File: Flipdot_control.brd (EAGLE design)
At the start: 160 x 100 mm, 24 parts, among them IC1 ULN2003, IC10 ULN2003, IC11 M74HC238, IC12 M74HC238, IC13 M74HC238, IC14 TD62783_AFWG, IC15 ULN2003, IC16 TD62783_AFWG, IC17 ULN2003, IC18 M74HC238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

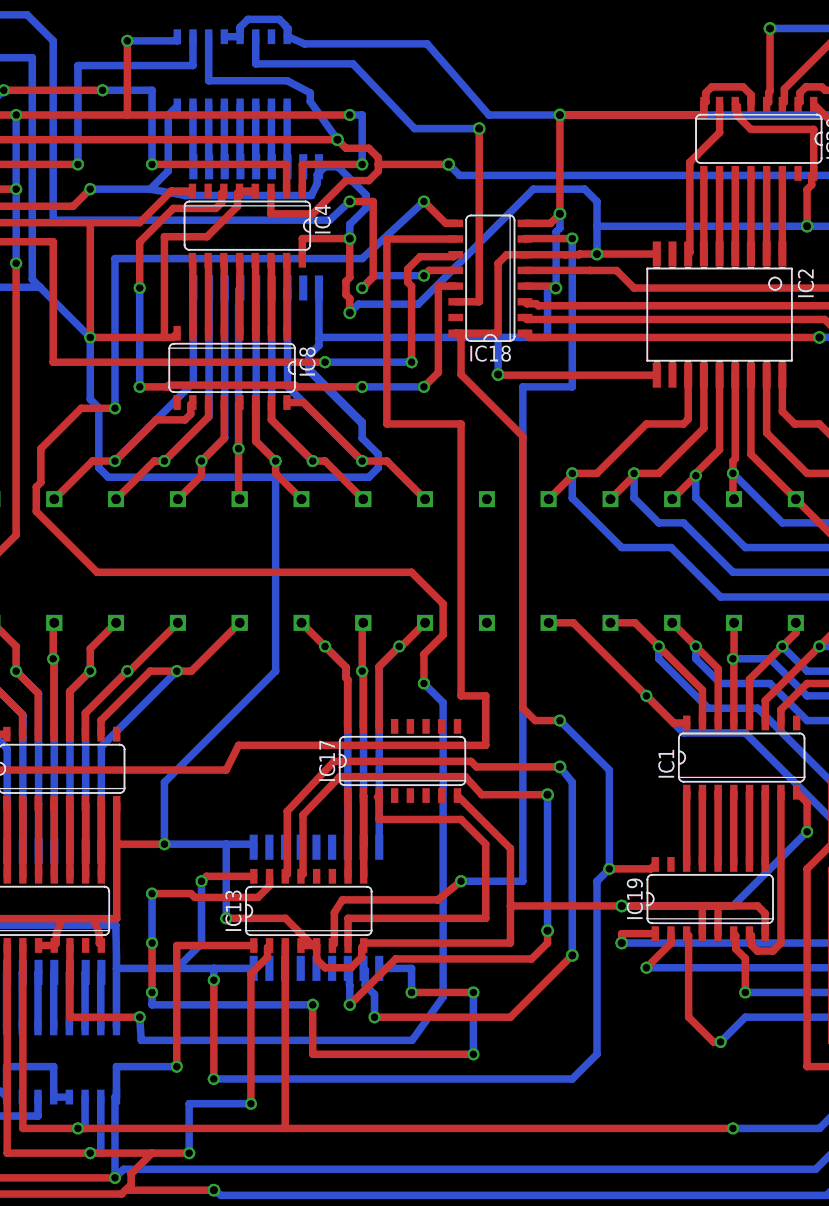
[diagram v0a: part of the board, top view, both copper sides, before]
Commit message: Fixed airwires
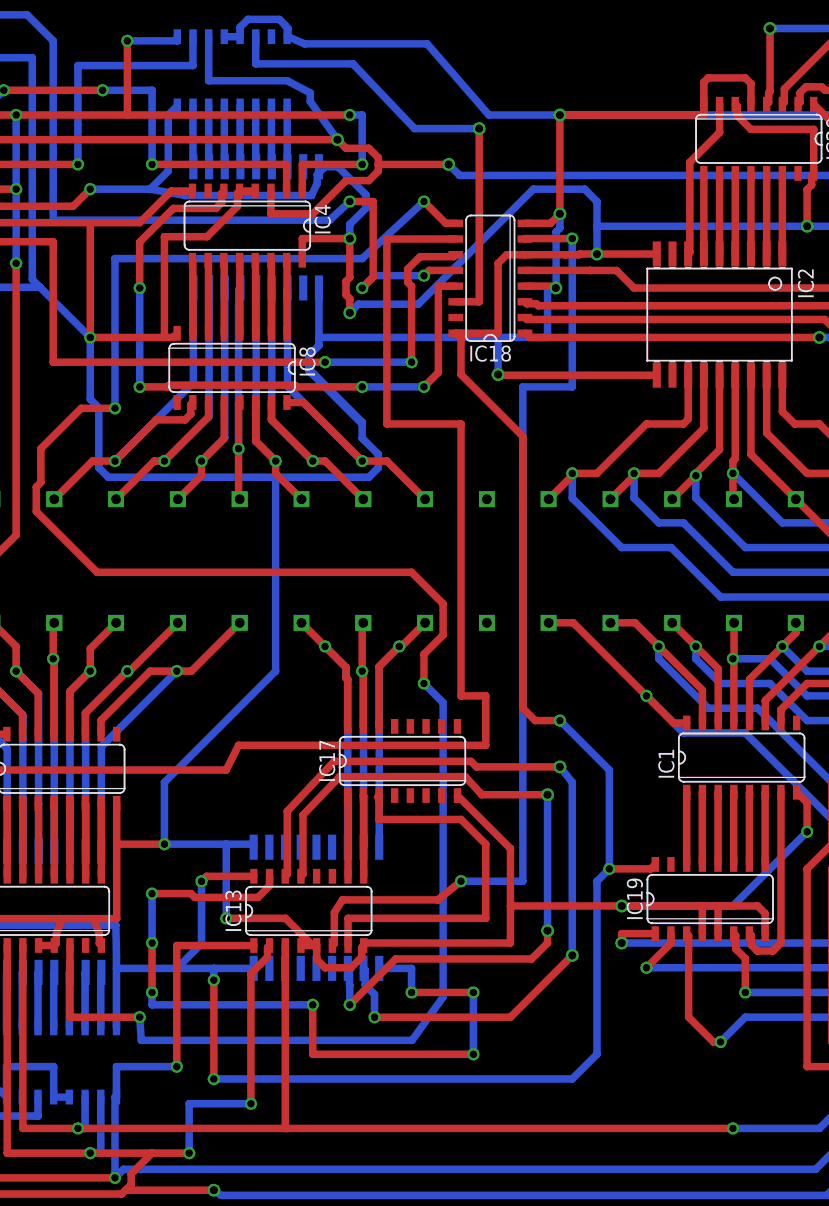
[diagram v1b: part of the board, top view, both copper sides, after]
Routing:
- net GND: track 642.8 -> 644.6 mm
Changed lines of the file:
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@@
 <contactref element="IC20" pad="8"/>
 <contactref element="IC20" pad="5"/>
-<wire x1="87.649" y1="90" x2="87.649" y2="90.873" width="0.6096" layer="1"/>
-<wire x1="87.8142" y1="91.80635625" x2="88.28564375" y2="92.2778" width="0.6096" layer="1"/>
-<wire x1="87.649" y1="90.873" x2="87.8142" y2="91.0382" width="0.6096" layer="1"/>
-<wire x1="87.8142" y1="91.0382" x2="87.8142" y2="91.80635625" width="0.6096" layer="1"/>
-<wire x1="88.28564375" y1="92.2778" x2="90.82235625" y2="92.2778" width="0.6096" layer="1"/>
-<wire x1="90.82235625" y1="92.2778" x2="91.4638" y2="91.63635625" width="0.6096" layer="1"/>
-<wire x1="91.4638" y1="91.63635625" x2="91.4638" y2="90.873" width="0.6096" layer="1"/>
+<wire x1="87.649" y1="90.873" x2="87.649" y2="90" width="0.6096" layer="1"/>
 <wire x1="31.23" y1="13" x2="31.23" y2="10.535" width="0.6096" layer="16"/>
 <wire x1="35.04" y1="10.535" x2="35.04" y2="13" width="0.6096" layer="16"/>
@@
 <wire x1="153" y1="83" x2="136" y2="83" width="0.6096" layer="16"/>
 <wire x1="136" y1="83" x2="136" y2="78.04" width="0.6096" layer="16"/>
-<wire x1="91.4638" y1="90.873" x2="91.459" y2="90.873" width="0" layer="19" extent="1-1"/>
+<wire x1="91.459" y1="90.873" x2="91.459" y2="92.541" width="0.6096" layer="1"/>
+<wire x1="91.459" y1="92.541" x2="91" y2="93" width="0.6096" layer="1"/>
+<wire x1="91" y1="93" x2="88" y2="93" width="0.6096" layer="1"/>
+<wire x1="88" y1="93" x2="87.649" y2="92.649" width="0.6096" layer="1"/>
+<wire x1="87.649" y1="92.649" x2="87.649" y2="90.873" width="0.6096" layer="1"/>
 </signal>
 <signal name="R7H">
@@
 <contactref element="IC2" pad="7"/>
 <wire x1="86.379" y1="78.7512" x2="86.514" y2="78.8862" width="0.6096" layer="1"/>
-<wire x1="88.9238" y1="88.58595625" x2="88.9238" y2="90.873" width="0.6096" layer="1"/>
 <wire x1="86.514" y1="78.8862" x2="86.514" y2="86.17615625" width="0.6096" layer="1"/>
-<wire x1="86.514" y1="86.17615625" x2="88.9238" y2="88.58595625" width="0.6096" layer="1"/>
-<wire x1="88.9238" y1="90.873" x2="88.919" y2="90.873" width="0" layer="19" extent="1-1"/>
+<wire x1="88.9238" y1="88.58595625" x2="86.514" y2="86.17615625" width="0.6096" layer="1"/>
+<wire x1="88.919" y1="90.873" x2="88.9238" y2="90.8682" width="0.6096" layer="1"/>
+<wire x1="88.9238" y1="90.8682" x2="88.9238" y2="88.58595625" width="0.6096" layer="1"/>
 </signal>
 <signal name="RE">
@@
 <wire x1="37" y1="8" x2="37.58" y2="8" width="0.6096" layer="16"/>
 <wire x1="37.58" y1="8" x2="37.58" y2="10.535" width="0.6096" layer="16"/>
-<wire x1="37" y1="8" x2="53.7732" y2="8" width="0.6096" layer="1"/>
-<wire x1="53.7732" y1="8" x2="53.7732" y2="22.799" width="0.6096" layer="1"/>
-<wire x1="53.7732" y1="8" x2="90" y2="8" width="0.6096" layer="1"/>
+<wire x1="54" y1="8" x2="37" y2="8" width="0.6096" layer="1"/>
+<wire x1="54" y1="8" x2="90" y2="8" width="0.6096" layer="1"/>
 <wire x1="121" y1="50" x2="121" y2="51.8727625" width="0.6096" layer="1"/>
 <wire x1="121" y1="51.8727625" x2="120.9554" y2="51.9173625" width="0.6096" layer="1"/>
@@
 <wire x1="152" y1="47" x2="154" y2="49" width="0.6096" layer="16"/>
 <wire x1="154" y1="49" x2="154" y2="49.78" width="0.6096" layer="16"/>
-<wire x1="53.7732" y1="22.799" x2="53.778" y2="22.799" width="0" layer="19" extent="1-1"/>
+<wire x1="53.778" y1="22.799" x2="53.778" y2="8" width="0.6096" layer="1"/>
+<wire x1="53.778" y1="8" x2="54" y2="8" width="0.6096" layer="1"/>
 </signal>
 <signal name="E1">

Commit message: Fucked up, fixed
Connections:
- net 12V: now also IC14.9, IC16.9, IC2.9, IC7.9, IC9.9
- net 5V: no longer IC14.9, IC16.9, IC2.9, IC7.9, IC9.9
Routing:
- net 12V: track 42.9 -> 377.1 mm, vias 2 -> 11
- net B: track 477.0 -> 449.4 mm, vias 14 -> 13
- net 5V: track 441.8 -> 458.9 mm, vias 21 -> 22
- net RE: track 148.8 -> 154.1 mm
- net C: track 396.7 -> 399.4 mm
- net A: track 430.0 -> 430.8 mm

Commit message: Finished segment schematic, fixed some errors
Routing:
- net 5V: track 458.9 -> 446.8 mm, vias 22 -> 21
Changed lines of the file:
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@@
 <layer number="19" name="Unrouted" color="6" fill="1" visible="yes" active="yes"/>
 <layer number="20" name="Dimension" color="15" fill="1" visible="yes" active="yes"/>
-<layer number="21" name="tPlace" color="7" fill="1" visible="no" active="yes"/>
+<layer number="21" name="tPlace" color="7" fill="1" visible="yes" active="yes"/>
 <layer number="22" name="bPlace" color="7" fill="1" visible="yes" active="yes"/>
-<layer number="23" name="tOrigins" color="15" fill="1" visible="no" active="yes"/>
+<layer number="23" name="tOrigins" color="15" fill="1" visible="yes" active="yes"/>
 <layer number="24" name="bOrigins" color="15" fill="1" visible="yes" active="yes"/>
-<layer number="25" name="tNames" color="7" fill="1" visible="no" active="yes"/>
+<layer number="25" name="tNames" color="7" fill="1" visible="yes" active="yes"/>
 <layer number="26" name="bNames" color="7" fill="1" visible="yes" active="yes"/>
-<layer number="27" name="tValues" color="7" fill="1" visible="no" active="yes"/>
+<layer number="27" name="tValues" color="7" fill="1" visible="yes" active="yes"/>
 <layer number="28" name="bValues" color="7" fill="1" visible="yes" active="yes"/>
 <layer number="29" name="tStop" color="7" fill="3" visible="no" active="yes"/>
@@
 <layer number="38" name="bTest" color="7" fill="1" visible="no" active="yes"/>
 <layer number="39" name="tKeepout" color="4" fill="11" visible="no" active="yes"/>
-<layer number="40" name="bKeepout" color="1" fill="11" visible="yes" active="yes"/>
+<layer number="40" name="bKeepout" color="1" fill="11" visible="no" active="yes"/>
 <layer number="41" name="tRestrict" color="4" fill="10" visible="no" active="yes"/>
-<layer number="42" name="bRestrict" color="1" fill="10" visible="yes" active="yes"/>
+<layer number="42" name="bRestrict" color="1" fill="10" visible="no" active="yes"/>
 <layer number="43" name="vRestrict" color="2" fill="10" visible="no" active="yes"/>
-<layer number="44" name="Drills" color="7" fill="1" visible="yes" active="yes"/>
-<layer number="45" name="Holes" color="7" fill="1" visible="yes" active="yes"/>
+<layer number="44" name="Drills" color="7" fill="1" visible="no" active="yes"/>
+<layer number="45" name="Holes" color="7" fill="1" visible="no" active="yes"/>
 <layer number="46" name="Milling" color="3" fill="1" visible="no" active="yes"/>
 <layer number="47" name="Measures" color="7" fill="1" visible="no" active="yes"/>
@@
 <layer number="49" name="Reference" color="7" fill="1" visible="no" active="yes"/>
 <layer number="50" name="dxf" color="7" fill="1" visible="no" active="no"/>
-<layer number="51" name="tDocu" color="7" fill="1" visible="no" active="yes"/>
+<layer number="51" name="tDocu" color="7" fill="1" visible="yes" active="yes"/>
 <layer number="52" name="bDocu" color="7" fill="1" visible="yes" active="yes"/>
 <layer number="53" name="tGND_GNDA" color="7" fill="9" visible="no" active="no"/>
@@
 <wire x1="30" y1="78" x2="30" y2="80.9682" width="0.6096" layer="16"/>
 <wire x1="30" y1="80.9682" x2="28.352203125" y2="82.615996875" width="0.6096" layer="16"/>
-<via x="25.127" y="89.508" extent="1-16" drill="0.6"/>
-<wire x1="13" y1="89.508" x2="25.127" y2="89.508" width="0.6096" layer="1"/>
 <via x="13" y="89.508" extent="1-16" drill="0.6"/>
 <wire x1="13" y1="89.508" x2="13" y2="90.379" width="0.6096" layer="16"/>

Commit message: Starting again [backup]
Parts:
- added U$1: PS, Flipdot:PS
- moved J1 14.0 mm to (46.1, 52.9)
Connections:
- net 12V: now also U$1.P$1, U$1.P$2
- net GND: now also U$1.P$3
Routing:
- net E6: track 163.6 -> 110.6 mm, vias 4 -> 3
- net A: track 430.8 -> 381.9 mm
- net E7: track 78.9 -> 38.9 mm
- net R5L: track 82.5 -> 119.8 mm
- net R4L: track 78.5 -> 115.2 mm
- net R6L: track 87.9 -> 124.3 mm
- net R3L: track 76.4 -> 112.3 mm
- net R7L: track 92.6 -> 126.9 mm
- net E5: track 147.1 -> 113.1 mm
- net R4H: track 111.1 -> 143.1 mm
- net 5V: track 446.8 -> 416.3 mm
- net R3H: track 116.0 -> 145.7 mm
- net R2L: track 88.3 -> 115.5 mm, vias 3 -> 4
- net R2H: track 119.3 -> 146.3 mm
- net R1L: track 101.3 -> 126.9 mm, vias 5 -> 6
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
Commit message: Finished new design
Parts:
- moved U$1 91.7 mm to (101.6, 9.63), turned to 90 degrees
- moved J2 67.3 mm to (84.4, 50.8), flipped to the bottom, turned to 180 degrees
- moved IC21 52.8 mm to (98.1, 62.0), turned to 0 degrees
- moved IC18 47.2 mm to (92.2, 35.0), flipped to the bottom, turned to 180 degrees
- moved IC19 35.7 mm to (52.8, 21.7)
- moved IC1 35.4 mm to (55.4, 35.0)
- moved IC20 35.3 mm to (57.0, 84.0)
- moved IC2 35.2 mm to (53.9, 71.1)
- moved IC17 21.5 mm to (42.0, 35.0)
- moved IC13 19.4 mm to (45.4, 9.15), turned to 270 degrees
- moved IC7 17.8 mm to (38.1, 69.1)
- moved MCU1 17.6 mm to (115.1, 76.8)
- moved IC3 17.4 mm to (36.2, 82.4)
- moved IC8 13.3 mm to (36.9, 65.3)
- moved IC4 13.2 mm to (38.1, 77.1)
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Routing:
- net E1: track 38.4 -> 204.0 mm, vias 1 -> 2
- net E2: track 53.8 -> 196.2 mm, vias 4 -> 3
- net R5H: track 150.6 -> 39.2 mm, vias 1 -> 2
- net B: track 448.9 -> 338.4 mm, vias 13 -> 12
- net R4H: track 143.1 -> 42.3 mm, vias 1 -> 2
- net R3H: track 145.7 -> 47.5 mm, vias 3 -> 2
- net E3: track 73.4 -> 168.7 mm, vias 3 -> 0
- net R7L: track 126.9 -> 32.0 mm, vias 3 -> 2
- net R2H: track 146.3 -> 52.7 mm, vias 3 -> 2
- net R6H: track 129.0 -> 35.8 mm, vias 1 -> 2
- net R7H: track 124.2 -> 31.6 mm, vias 1 -> 2
- net C: track 399.4 -> 309.2 mm, vias 12 -> 10
- net R6L: track 124.3 -> 35.2 mm, vias 3 -> 2
- net R1H: track 142.5 -> 56.7 mm, vias 4 -> 2
- net R5L: track 119.8 -> 38.4 mm, vias 3 -> 2
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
